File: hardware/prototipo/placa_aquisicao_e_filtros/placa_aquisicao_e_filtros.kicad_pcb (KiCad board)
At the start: 2 copper layers, 47 parts, among them J1 Conn_01x02, J2 Conn_01x04, J3 Conn_02x04_Counter_Clockwise, J4 Conn_01x02, J5 Conn_01x02, J6 Conn_01x02, Q1 BF245B, U1 AP1117-33, U2 TPS60401, U3 Opamp_Quad_Generic, U4 AD620, U5 Opamp_Quad_Generic

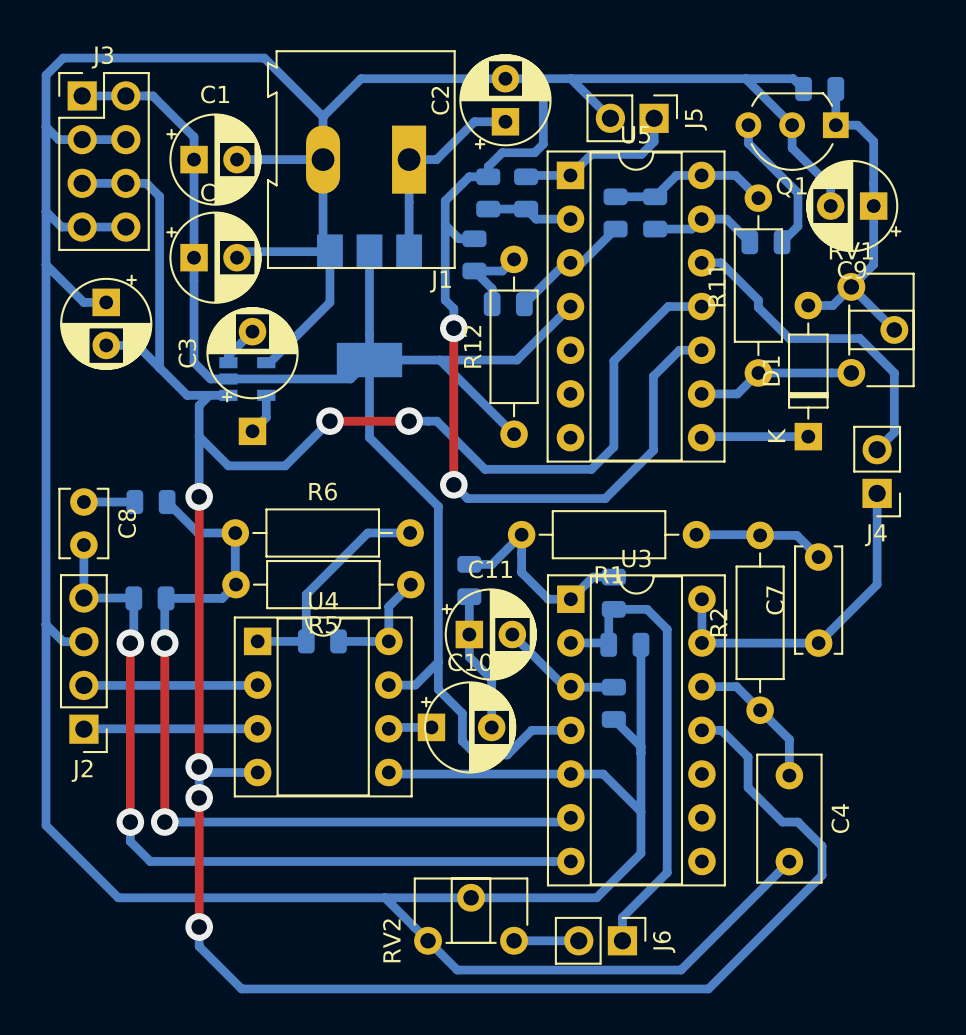
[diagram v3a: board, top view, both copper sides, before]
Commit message: Second prototype working with bluetooth.
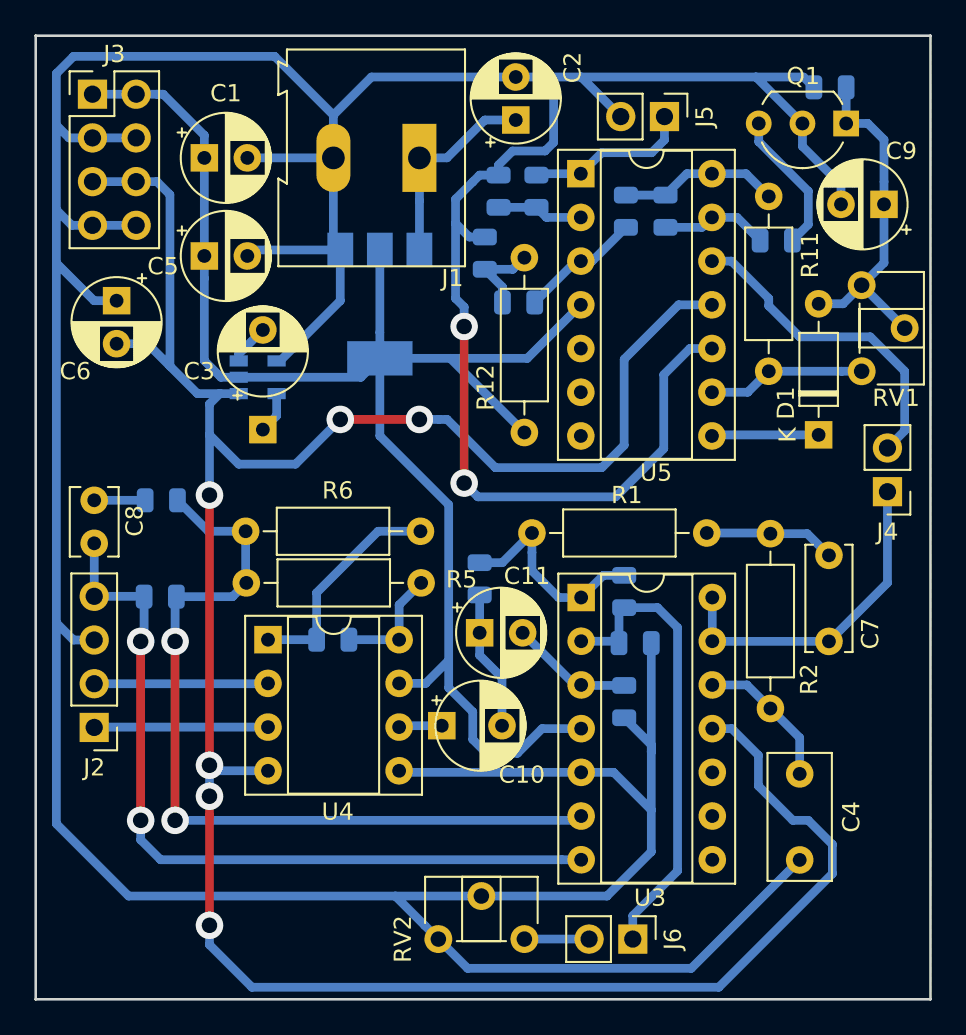
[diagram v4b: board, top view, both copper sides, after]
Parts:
- moved C5 0.61 mm to (136.8, 33.8)
- moved J3 0.61 mm to (130.3, 24.4)
- moved R14 0.61 mm to (161.3, 31.2)
- moved R19 0.61 mm to (152.8, 52.6)
- moved R3 0.61 mm to (134.2, 53.6)
- moved R4 0.61 mm to (134.3, 48.0)
- moved C1 0.61 mm to (136.8, 28.1)
- moved C9 0.61 mm to (176.3, 30.8)
- moved J1 0.61 mm to (149.3, 28.1)
- moved C11 0.61 mm to (152.8, 55.7)
- moved C10 0.61 mm to (151.6, 61.1)
- moved C2 0.61 mm to (154.9, 25.9)
- moved C3 0.61 mm to (140.2, 40.6)
- moved C4 0.61 mm to (171.4, 63.9)
- moved C6 0.61 mm to (131.7, 36.4)
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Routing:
- added copper zone on B.Cu, net GNDA
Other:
- board outline added: 52 x 56 mm
